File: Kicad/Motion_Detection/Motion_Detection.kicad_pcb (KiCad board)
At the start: 2 copper layers, 66.7 x 51.4 mm, 19 parts, among them J1 SEN0192_MW, J2 SE-10, J3 12V input, J4 5V Ext, J5 3V3 EN, J6 ZRE200GE, J7 EKMB, J8 3V3 Output, P1 XBee, U1 LM324, U2 LM7805_TO220

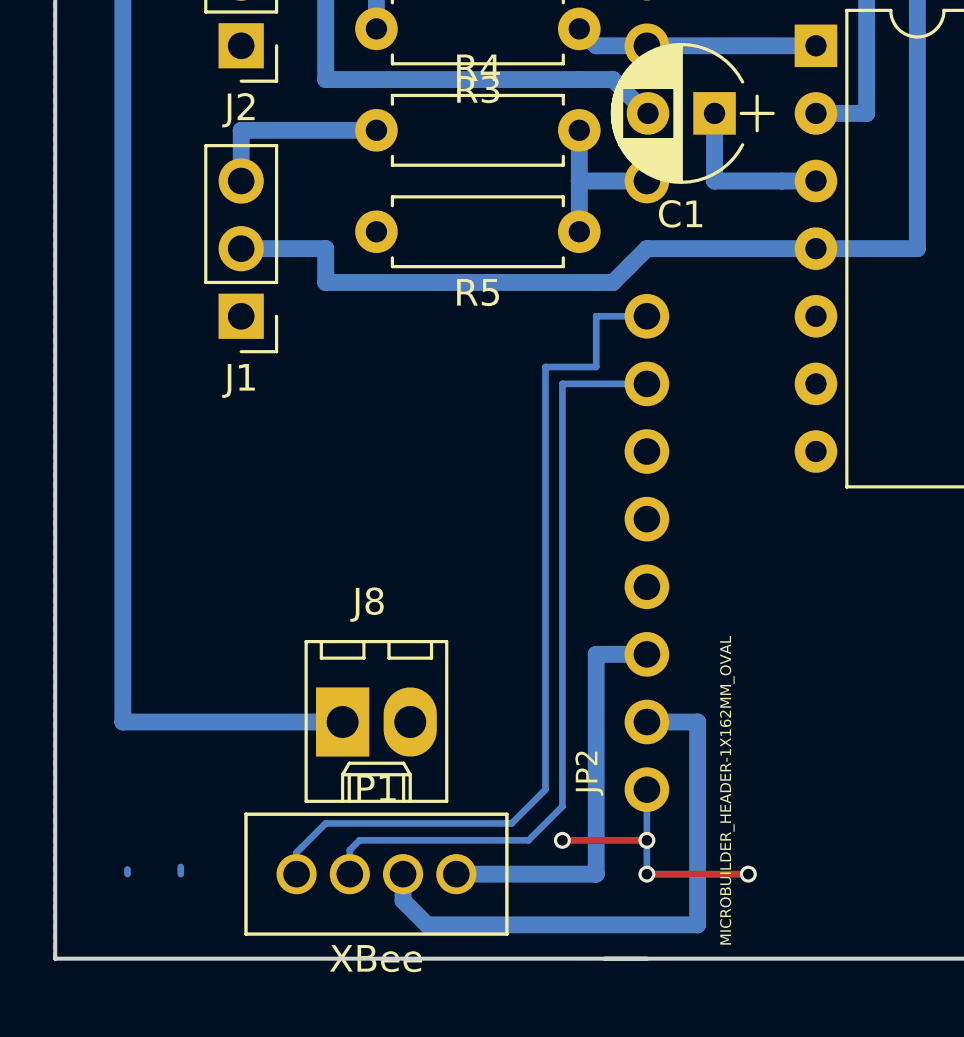
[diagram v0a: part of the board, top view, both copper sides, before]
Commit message: Updated Kicad Motion detection circuit and board. Updated Feather code to comunicate using XBee.
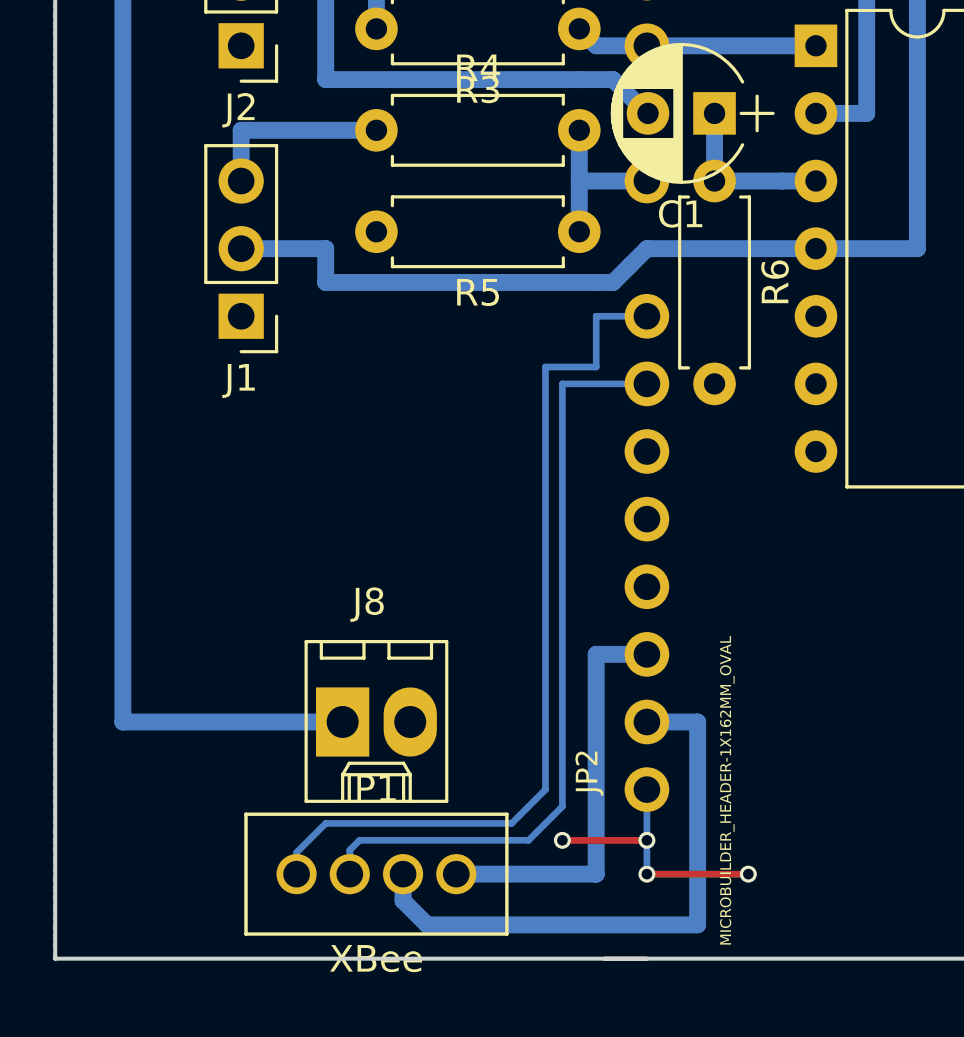
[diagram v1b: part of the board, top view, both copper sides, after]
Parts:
- added R6: 4.62K, Resistors_THT:R_Axial_DIN0207_L6.3mm_D2.5mm_P7.62mm_Horizontal, F.Cu at (144.1, 95.9)
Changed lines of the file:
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@@
 (kicad_pcb (version 4) (host pcbnew 4.0.7-e2-6376~58~ubuntu16.04.1)
   (general
-    (links 37)
-    (no_connects 16)
+    (links 39)
+    (no_connects 17)
     (area 119.304999 73.584999 186.130001 125.170001)
     (thickness 1.6)
-    (drawings 10)
-    (tracks 76)
+    (drawings 14)
+    (tracks 74)
     (zones 0)
-    (modules 19)
+    (modules 20)
     (nets 19)
   )
@@
     )
   )
+  (module Resistors_THT:R_Axial_DIN0207_L6.3mm_D2.5mm_P7.62mm_Horizontal (layer F.Cu)
+    (at 144.145 95.885 270)
+    (descr "Resistor, Axial_DIN0207 series, Axial, Horizontal, pin pitch=7.62mm, 0.25W = 1/4W, length*diameter=6.3*2.5mm^2, http://cdn-reichelt.de/documents/datenblatt/B400/1_4W%23YAG.pdf")
+    (tags "Resistor Axial_DIN0207 series Axial Horizontal pin pitch 7.62mm 0.25W = 1/4W length 6.3mm diameter 2.5mm")
+    (fp_text reference R6 (at 3.81 -2.31 270) (layer F.SilkS)
+      (effects (font (size 1 1) (thickness 0.15)))
+    )
+    (fp_text value 4.62K (at 3.81 2.31 270) (layer F.Fab)
+      (effects (font (size 1 1) (thickness 0.15)))
+    )
+    (fp_line (start 0.66 -1.25) (end 0.66 1.25) (layer F.Fab) (width 0.1))
+    (fp_line (start 0.66 1.25) (end 6.96 1.25) (layer F.Fab) (width 0.1))
+    (fp_line (start 6.96 1.25) (end 6.96 -1.25) (layer F.Fab) (width 0.1))
+    (fp_line (start 6.96 -1.25) (end 0.66 -1.25) (layer F.Fab) (width 0.1))
+    (fp_line (start 0 0) (end 0.66 0) (layer F.Fab) (width 0.1))
+    (fp_line (start 7.62 0) (end 6.96 0) (layer F.Fab) (width 0.1))
+    (fp_line (start 0.6 -0.98) (end 0.6 -1.31) (layer F.SilkS) (width 0.12))
+    (fp_line (start 0.6 -1.31) (end 7.02 -1.31) (layer F.SilkS) (width 0.12))
+    (fp_line (start 7.02 -1.31) (end 7.02 -0.98) (layer F.SilkS) (width 0.12))
+    (fp_line (start 0.6 0.98) (end 0.6 1.31) (layer F.SilkS) (width 0.12))
+    (fp_line (start 0.6 1.31) (end 7.02 1.31) (layer F.SilkS) (width 0.12))
+    (fp_line (start 7.02 1.31) (end 7.02 0.98) (layer F.SilkS) (width 0.12))
+    (fp_line (start -1.05 -1.6) (end -1.05 1.6) (layer F.CrtYd) (width 0.05))
+    (fp_line (start -1.05 1.6) (end 8.7 1.6) (layer F.CrtYd) (width 0.05))
+    (fp_line (start 8.7 1.6) (end 8.7 -1.6) (layer F.CrtYd) (width 0.05))
+    (fp_line (start 8.7 -1.6) (end -1.05 -1.6) (layer F.CrtYd) (width 0.05))
+    (pad 1 thru_hole circle (at 0 0 270) (size 1.6 1.6) (drill 0.8) (layers *.Cu *.Mask)
+      (net 10 "Net-(C1-Pad1)"))
+    (pad 2 thru_hole oval (at 7.62 0 270) (size 1.6 1.6) (drill 0.8) (layers *.Cu *.Mask)
+      (net 1 GND))
+    (model ${KISYS3DMOD}/Resistors_THT.3dshapes/R_Axial_DIN0207_L6.3mm_D2.5mm_P7.62mm_Horizontal.wrl
+      (at (xyz 0 0 0))
+      (scale (xyz 0.393701 0.393701 0.393701))
+      (rotate (xyz 0 0 0))
+    )
+  )
+  (target plus (at 122.555 76.835) (size 5) (width 0.15) (layer Edge.Cuts))
+  (target plus (at 182.88 76.835) (size 5) (width 0.15) (layer Edge.Cuts))
+  (target plus (at 182.88 121.92) (size 5) (width 0.15) (layer Edge.Cuts))
+  (target plus (at 122.555 121.92) (size 5) (width 0.15) (layer Edge.Cuts))
   (gr_line (start 119.38 125.095) (end 119.38 73.66) (angle 90) (layer Edge.Cuts) (width 0.15))
   (gr_line (start 186.055 125.095) (end 186.055 73.66) (angle 90) (layer Edge.Cuts) (width 0.15))
@@
   (gr_line (start 140.0175 73.66) (end 163.5125 73.66) (angle 90) (layer Edge.Cuts) (width 0.15))
   (gr_line (start 163.5125 125.095) (end 140.0175 125.095) (angle 90) (layer Edge.Cuts) (width 0.15))
-  (segment (start 122.095 121.92) (end 122.095 121.745) (width 0.25) (layer B.Cu) (net 0) (status 30))
-  (segment (start 124.095 121.92) (end 124.095 121.65) (width 0.25) (layer B.Cu) (net 0) (status 30))
   (segment (start 141.605 118.745) (end 141.605 120.65) (width 0.25) (layer B.Cu) (net 1))
   (via (at 141.605 120.65) (size 0.635) (drill 0.4) (layers F.Cu B.Cu) (net 1))
@@
   (segment (start 144.145 95.885) (end 144.145 93.345) (width 0.635) (layer B.Cu) (net 10) (status 20))
   (segment (start 146.685 95.885) (end 144.145 95.885) (width 0.635) (layer B.Cu) (net 10))
-  (segment (start 160.02 83.82) (end 160.02 95.885) (width 0.635) (layer B.Cu) (net 11) (status 400000))
-  (segment (start 160.02 95.885) (end 161.925 95.885) (width 0.635) (layer B.Cu) (net 11) (status 800000))
-  (segment (start 164.465 83.82) (end 161.925 83.82) (width 0.25) (layer B.Cu) (net 12) (status 400000))
-  (segment (start 161.925 83.82) (end 161.925 93.345) (width 0.25) (layer B.Cu) (net 12) (status 800000))
+  (segment (start 160.02 83.82) (end 160.02 95.885) (width 0.635) (layer B.Cu) (net 11))
+  (segment (start 160.02 95.885) (end 161.925 95.885) (width 0.635) (layer B.Cu) (net 11))
+  (segment (start 164.465 83.82) (end 161.925 83.82) (width 0.25) (layer B.Cu) (net 12))
+  (segment (start 161.925 83.82) (end 161.925 93.345) (width 0.25) (layer B.Cu) (net 12))
   (segment (start 132.445 121.92) (end 132.445 122.92) (width 0.635) (layer B.Cu) (net 14))
   (segment (start 143.51 116.205) (end 141.605 116.205) (width 0.635) (layer B.Cu) (net 14))

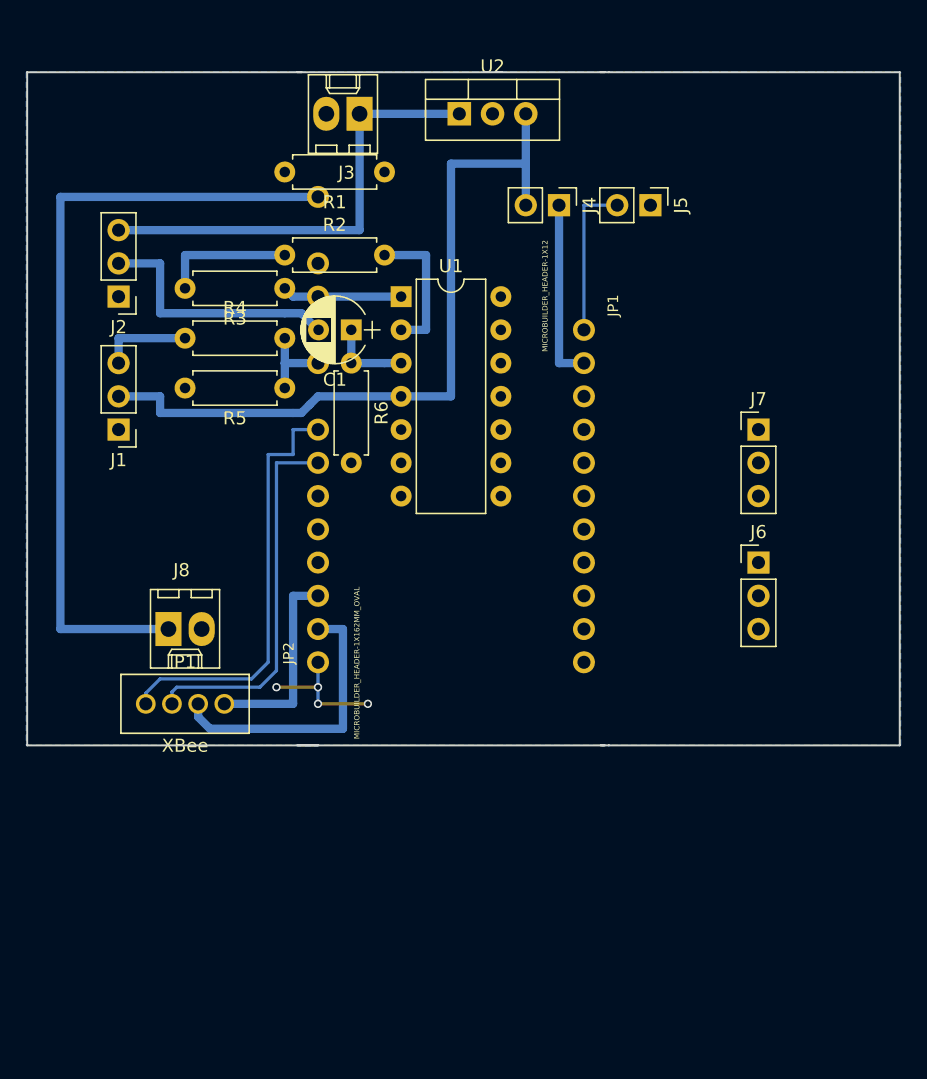
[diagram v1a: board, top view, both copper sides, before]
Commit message: Two new signal conditioning stages were added and the final pcb layout completed.
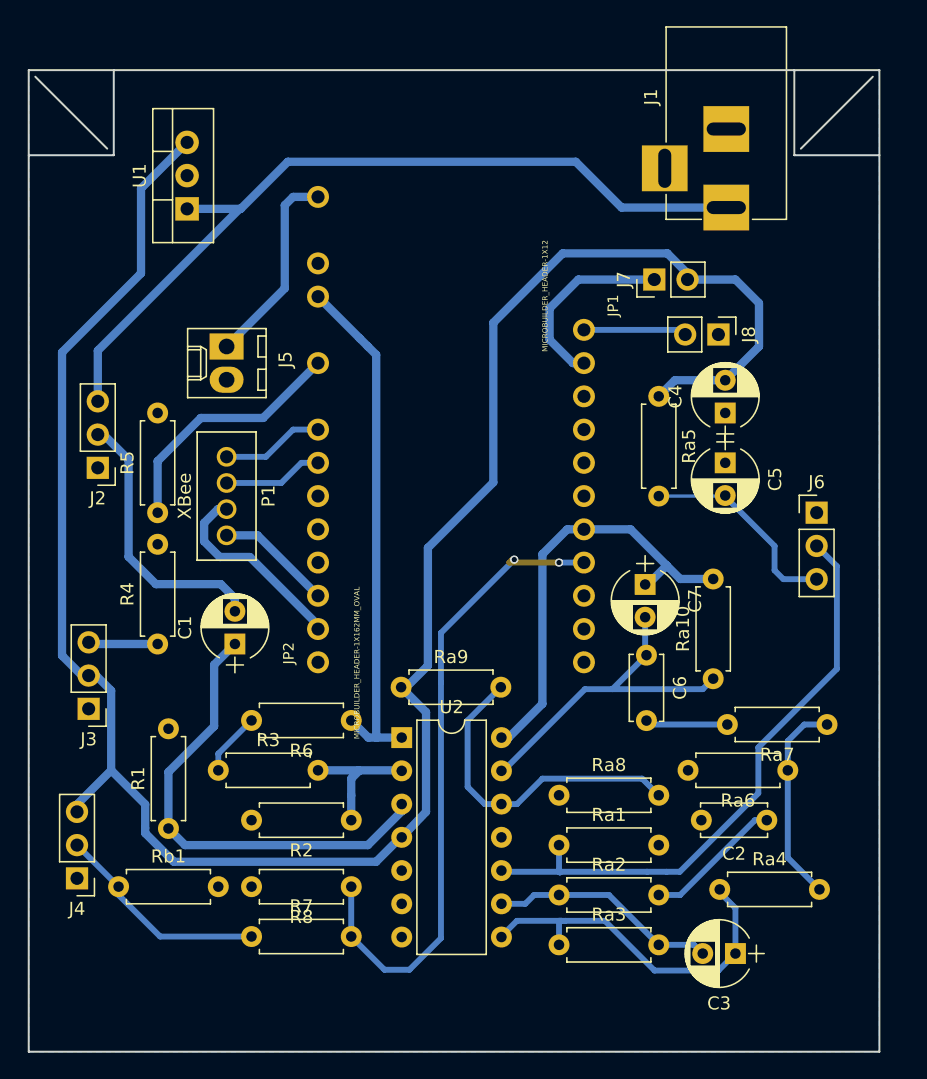
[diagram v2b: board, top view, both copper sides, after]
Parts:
- added C2: 10u, Capacitors_THT:C_Disc_D5.0mm_W2.5mm_P5.00mm, F.Cu at (175.9, 130.8)
- added C3: 10n, Capacitors_THT:CP_Radial_D5.0mm_P2.50mm, F.Cu at (173.5, 141.0)
- added C4: 100u, Capacitors_THT:CP_Radial_D5.0mm_P2.50mm, F.Cu at (172.7, 99.7)
- added C5: 10u, Capacitors_THT:CP_Radial_D5.0mm_P2.50mm, F.Cu at (172.7, 103.5)
- added C6: 10u, Capacitors_THT:C_Disc_D5.0mm_W2.5mm_P5.00mm, F.Cu at (166.7, 118.2)
- added C7: 10n, Capacitors_THT:CP_Radial_D5.0mm_P2.50mm, F.Cu at (166.6, 112.8)
- added R7: 1.491K, Resistors_THT:R_Axial_DIN0207_L6.3mm_D2.5mm_P7.62mm_Horizontal, F.Cu at (136.5, 139.7)
- added R8: 2.18K, Resistors_THT:R_Axial_DIN0207_L6.3mm_D2.5mm_P7.62mm_Horizontal, F.Cu at (144.1, 135.9)
- added Ra1: 47K, Resistors_THT:R_Axial_DIN0207_L6.3mm_D2.5mm_P7.62mm_Horizontal, F.Cu at (160.0, 132.7)
- added Ra10: 1M2, Resistors_THT:R_Axial_DIN0207_L6.3mm_D2.5mm_P7.62mm_Horizontal, F.Cu at (171.8, 120.0)
- added Ra2: 10K, Resistors_THT:R_Axial_DIN0207_L6.3mm_D2.5mm_P7.62mm_Horizontal, F.Cu at (160.0, 136.5)
- added Ra3: 1M, Resistors_THT:R_Axial_DIN0207_L6.3mm_D2.5mm_P7.62mm_Horizontal, F.Cu at (160.0, 140.3)
- added Ra4: 100K, Resistors_THT:R_Axial_DIN0207_L6.3mm_D2.5mm_P7.62mm_Horizontal, F.Cu at (172.3, 136.1)
- added Ra5: 1K, Resistors_THT:R_Axial_DIN0207_L6.3mm_D2.5mm_P7.62mm_Horizontal, F.Cu at (167.6, 98.4)
- added Ra6: 1M, Resistors_THT:R_Axial_DIN0207_L6.3mm_D2.5mm_P7.62mm_Horizontal, F.Cu at (177.5, 127.0)
- added Ra7: 10K, Resistors_THT:R_Axial_DIN0207_L6.3mm_D2.5mm_P7.62mm_Horizontal, F.Cu at (180.5, 123.5)
- added Ra8: 470K, Resistors_THT:R_Axial_DIN0207_L6.3mm_D2.5mm_P7.62mm_Horizontal, F.Cu at (160.0, 128.9)
- added Ra9: 810K, Resistors_THT:R_Axial_DIN0207_L6.3mm_D2.5mm_P7.62mm_Horizontal, F.Cu at (148.0, 120.7)
- added Rb1: 10K, Resistors_THT:R_Axial_DIN0207_L6.3mm_D2.5mm_P7.62mm_Horizontal, F.Cu at (126.4, 135.9)
- J1: value SEN0192_MW -> 12V input; footprint Pin_Headers:Pin_Header_Straight_1x03_Pitch2.54mm -> Connectors:BARREL_JACK
- J3: value 12V input -> SEN0192_MW; footprint Connectors_Molex:Molex_KK-6410-02_02x2.54mm_Straight -> Pin_Headers:Pin_Header_Straight_1x03_Pitch2.54mm
- J4: value 5V Ext -> EKMB; footprint Pin_Headers:Pin_Header_Straight_1x02_Pitch2.54mm -> Pin_Headers:Pin_Header_Straight_1x03_Pitch2.54mm
- J5: value 3V3 EN -> 3V3 Output; footprint Pin_Headers:Pin_Header_Straight_1x02_Pitch2.54mm -> Connectors_Molex:Molex_KK-6410-02_02x2.54mm_Straight
- J7: value EKMB -> 5V Ext; footprint Pin_Headers:Pin_Header_Straight_1x03_Pitch2.54mm -> Pin_Headers:Pin_Header_Straight_1x02_Pitch2.54mm
- J8: value 3V3 Output -> 3V3 EN; footprint Connectors_Molex:Molex_KK-6410-02_02x2.54mm_Straight -> Pin_Headers:Pin_Header_Straight_1x02_Pitch2.54mm
- R1: value 9.85K -> 4.62K
- R2: value 9.87K -> 9.85K
- R3: value 14.82K -> 9.87K
- R6: value 4.62K -> 14.82K
- U1: value LM324 -> LM7805_TO220; footprint Housings_DIP:DIP-14_W7.62mm -> TO_SOT_Packages_THT:TO-220-3_Vertical
- U2: value LM7805_TO220 -> LM324; footprint TO_SOT_Packages_THT:TO-220-3_Vertical -> Housings_DIP:DIP-14_W7.62mm
- moved J4 63.3 mm to (123.2, 135.3), turned to 180 degrees
- moved R1 52.8 mm to (130.2, 131.4), turned to 90 degrees
- moved J3 50.0 mm to (124.1, 122.3)
- moved J1 49.4 mm to (172.8, 84.0), turned to 270 degrees
- moved U2 47.9 mm to (148.0, 124.5)
- moved J8 47.7 mm to (172.2, 93.7), turned to 270 degrees
- moved R2 43.5 mm to (144.1, 130.8), turned to 180 degrees
- moved R3 37.2 mm to (134.0, 127.0), turned to 0 degrees
- moved J5 34.1 mm to (134.6, 94.6)
- moved R6 27.3 mm to (144.1, 123.2), turned to 180 degrees
- moved C1 25.6 mm to (135.3, 117.3), turned to 90 degrees
- moved R4 23.5 mm to (129.3, 117.3), turned to 90 degrees
- moved U1 17.7 mm to (131.6, 84.1), turned to 90 degrees
- moved P1 16.2 mm to (134.6, 106.0), turned to 270 degrees
- moved J7 14.0 mm to (167.3, 89.5), turned to 90 degrees
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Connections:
- J1 pad 1: GND -> 12V
- J1 pad 2: 5V -> GND
- J1 pad 3: SEN0192_OUT -> GND
- J3 pad 1: 12V -> GND
- J3 pad 2: GND -> 5V
- J4 pad 1: VBUS -> GND
- J4 pad 2: 5V -> EKMB_OUT
- J5 pad 1: GND -> 3V3
- J5 pad 2: EN -> GND
- J6 pad 2: (no net) -> ZRE200_OUT
- J6 pad 3: 5V -> Net-(C5-Pad2)
- J7 pad 1: GND -> VBUS
- J7 pad 2: (no net) -> 5V
- J8 pad 1: 3V3 -> GND
- J8 pad 2: GND -> EN
- JP1 pad 7: ZRE200_OUT_ -> (no net)
- JP1 pad 8: (no net) -> ZRE200_OUT_
- JP1 pad 9: (no net) -> EKMB_OUT_
- R1 pad 1: Net-(R1-Pad1) -> Net-(C1-Pad1)
- R2 pad 2: Net-(R1-Pad1) -> GND
- R3 pad 1: SE-10_OUT_ -> Net-(R3-Pad1)
- R6 pad 1: Net-(C1-Pad1) -> SE-10_OUT_
- R6 pad 2: GND -> Net-(R3-Pad1)
- U1 pad 1: SE-10_OUT_ -> 12V
- U1 pad 2: Net-(R1-Pad1) -> GND
- U1 pad 3: Net-(C1-Pad1) -> 5V
- U2 pad 1: 12V -> SE-10_OUT_
- U2 pad 2: GND -> Net-(R2-Pad1)
- U2 pad 3: 5V -> Net-(C1-Pad1)
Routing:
- net 5V: track 57.7 -> 166.6 mm
- net EKMB_OUT_: track 0.00 -> 50.1 mm, vias 0 -> 2
- net ZRE200_OUT: track 0.00 -> 46.8 mm
- net 3V3: track 61.0 -> 15.4 mm
- net ZRE200_OUT_: track 0.00 -> 33.3 mm
- net SE-10_OUT_: track 9.15 -> 40.0 mm
- net Net-(C1-Pad1): track 6.35 -> 36.8 mm
- net Net-(C3-Pad1): track 0.00 -> 28.2 mm
- net 12V: track 35.6 -> 63.4 mm
- net Net-(C6-Pad1): track 0.00 -> 26.5 mm
- net Net-(Ra8-Pad2): track 0.00 -> 25.2 mm
- net XBee_ON: track 32.7 -> 7.85 mm
- net XBee_nRESET: track 28.6 -> 7.62 mm
- net Net-(C3-Pad2): track 0.00 -> 17.5 mm
- net EKMB_OUT: track 0.00 -> 16.6 mm
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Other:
- board size 66.7 x 51.4 mm -> 65 x 75 mm
- net class Default: trace_width 0.25 -> 0.45
